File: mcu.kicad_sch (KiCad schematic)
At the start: 33 parts, among them J301 CONN_MCU_SERIAL, J302 CONN_EXT, SW301 SW_RST, SW302 SW_BOOT0, U301 STM32F765IITx, Y301 25MHz

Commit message: Fully update PCB and schematic after BOM consolidation
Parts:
- C301, C302, C303, C304, C305, C306, C307, C308, C309, C310, C311, C312, C313, C314, C315, C316: Part (none) -> 603-CC603ZRY5V7BB104
- C317, C318: Part (none) -> 187-CL10A225KQ8NNNC
- C319, C320: Part (none) -> 187-CL10C120JB81PNC
- R301, R302, R303: Part (none) -> 791-RMC1/16-1002FTP
- R304: Part (none) -> 791-RMC1/16-221JTP
- R305, R306, R307: Part (none) -> 652-CR0603-J/-000ELF
- SW301, SW302: Part (none) -> 113-DTSMW-69N-V-T/R
- Y301: Part (none) -> 815-ABM3B-25-B2
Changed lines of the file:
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@@
+      (effects (font (size 1.27 1.27)) hide)
+    )
+    (property "Part" "791-RMC1/16-221JTP" (id 4) (at 125.73 166.37 0)
       (effects (font (size 1.27 1.27)) hide)
     )
@@
     )
     (property "Datasheet" "~" (id 3) (at 203.835 160.02 0)
+      (effects (font (size 1.27 1.27)) hide)
+    )
+    (property "Part" "652-CR0603-J/-000ELF" (id 4) (at 203.835 160.02 0)
       (effects (font (size 1.27 1.27)) hide)
     )
@@
       (effects (font (size 1.27 1.27)) hide)
     )
+    (property "Part" "791-RMC1/16-1002FTP" (id 4) (at 39.37 134.62 0)
+      (effects (font (size 1.27 1.27)) hide)
+    )
     (pin "1")
     (pin "2")
@@
       (effects (font (size 1.27 1.27)) hide)
     )
+    (property "Part" "791-RMC1/16-1002FTP" (id 4) (at 39.37 144.78 0)
+      (effects (font (size 1.27 1.27)) hide)
+    )
     (pin "1")
     (pin "2")
@@
       (effects (font (size 1.27 1.27)) hide)
     )
+    (property "Part" "603-CC603ZRY5V7BB104" (id 4) (at 34.29 93.98 0)
+      (effects (font (size 1.27 1.27)) hide)
+    )
     (pin "1")
     (pin "2")
@@
       (effects (font (size 1.27 1.27)) hide)
     )
+    (property "Part" "791-RMC1/16-1002FTP" (id 4) (at 39.37 139.7 0)
+      (effects (font (size 1.27 1.27)) hide)
+    )
     (pin "1")
     (pin "2")
@@
     )
     (property "Datasheet" "~" (id 3) (at 29.21 109.22 0)
+      (effects (font (size 1.27 1.27)) hide)
+    )
+    (property "Part" "603-CC603ZRY5V7BB104" (id 4) (at 29.21 109.22 0)
       (effects (font (size 1.27 1.27)) hide)
     )
@@
       (effects (font (size 1.27 1.27)) hide)
     )
+    (property "Part" "603-CC603ZRY5V7BB104" (id 4) (at 29.21 68.58 0)
+      (effects (font (size 1.27 1.27)) hide)
+    )
     (pin "1")
     (pin "2")
@@
     )
     (property "Datasheet" "~" (id 3) (at 115.57 182.88 0)
+      (effects (font (size 1.27 1.27)) hide)
+    )
+    (property "Part" "187-CL10C120JB81PNC" (id 4) (at 115.57 182.88 0)
       (effects (font (size 1.27 1.27)) hide)
     )
@@
     )
     (property "Datasheet" "~" (id 3) (at 57.15 157.48 0)
+      (effects (font (size 1.27 1.27)) hide)
+    )
+    (property "Part" "113-DTSMW-69N-V-T/R" (id 4) (at 62.23 157.48 0)
       (effects (font (size 1.27 1.27)) hide)
     )
@@
       (effects (font (size 1.27 1.27)) hide)
     )
+    (property "Part" "603-CC603ZRY5V7BB104" (id 4) (at 29.21 58.42 0)
+      (effects (font (size 1.27 1.27)) hide)
+    )
     (pin "1")
     (pin "2")
@@
       (effects (font (size 1.27 1.27)) hide)
     )
+    (property "Part" "603-CC603ZRY5V7BB104" (id 4) (at 34.29 104.14 0)
+      (effects (font (size 1.27 1.27)) hide)
+    )
     (pin "1")
     (pin "2")
@@
     )
     (property "Datasheet" "~" (id 3) (at 77.47 135.89 0)
+      (effects (font (size 1.27 1.27)) hide)
+    )
+    (property "Part" "187-CL10A225KQ8NNNC" (id 4) (at 77.47 135.89 0)
       (effects (font (size 1.27 1.27)) hide)
     )
@@
       (effects (font (size 1.27 1.27)) hide)
     )
+    (property "Part" "603-CC603ZRY5V7BB104" (id 4) (at 29.21 88.9 0)
+      (effects (font (size 1.27 1.27)) hide)
+    )
     (pin "1")
     (pin "2")
@@
       (effects (font (size 1.27 1.27)) hide)
     )
+    (property "Part" "187-CL10A225KQ8NNNC" (id 4) (at 67.31 135.89 0)
+      (effects (font (size 1.27 1.27)) hide)
+    )
     (pin "1")
     (pin "2")
@@
     )
     (property "Datasheet" "~" (id 3) (at 125.73 182.88 0)
+      (effects (font (size 1.27 1.27)) hide)
+    )
+    (property "Part" "187-CL10C120JB81PNC" (id 4) (at 125.73 182.88 0)
       (effects (font (size 1.27 1.27)) hide)
     )
@@
     )
     (property "Datasheet" "~" (id 3) (at 200.025 154.94 0)
+      (effects (font (size 1.27 1.27)) hide)
+    )
+    (property "Part" "652-CR0603-J/-000ELF" (id 4) (at 200.025 154.94 0)
       (effects (font (size 1.27 1.27)) hide)
     )
@@
       (effects (font (size 1.27 1.27)) hide)
     )
+    (property "Part" "603-CC603ZRY5V7BB104" (id 4) (at 39.37 151.13 0)
+      (effects (font (size 1.27 1.27)) hide)
+    )
     (pin "1")
     (pin "2")
@@
       (effects (font (size 1.27 1.27)) hide)
     )
+    (property "Part" "603-CC603ZRY5V7BB104" (id 4) (at 34.29 43.18 0)
+      (effects (font (size 1.27 1.27)) hide)
+    )
     (pin "1")
     (pin "2")
@@
       (effects (font (size 1.27 1.27)) hide)
     )
+    (property "Part" "603-CC603ZRY5V7BB104" (id 4) (at 34.29 114.3 0)
+      (effects (font (size 1.27 1.27)) hide)
+    )
     (pin "1")
     (pin "2")
@@
       (effects (font (size 1.27 1.27)) hide)
     )
+    (property "Part" "603-CC603ZRY5V7BB104" (id 4) (at 34.29 83.82 0)
+      (effects (font (size 1.27 1.27)) hide)
+    )
     (pin "1")
     (pin "2")
@@
     )
     (property "Datasheet" "~" (id 3) (at 29.21 99.06 0)
+      (effects (font (size 1.27 1.27)) hide)
+    )
+    (property "Part" "603-CC603ZRY5V7BB104" (id 4) (at 29.21 99.06 0)
       (effects (font (size 1.27 1.27)) hide)
     )
@@
       (effects (font (size 1.27 1.27)) hide)
     )
+    (property "Part" "603-CC603ZRY5V7BB104" (id 4) (at 34.29 53.34 0)
+      (effects (font (size 1.27 1.27)) hide)
+    )
     (pin "1")
     (pin "2")
@@
     )
     (property "Datasheet" "~" (id 3) (at 120.65 175.26 0)
+      (effects (font (size 1.27 1.27)) hide)
+    )
+    (property "Part" "815-ABM3B-25-B2" (id 4) (at 120.65 175.26 0)
       (effects (font (size 1.27 1.27)) hide)
     )
@@
       (effects (font (size 1.27 1.27)) hide)
     )
+    (property "Part" "603-CC603ZRY5V7BB104" (id 4) (at 29.21 48.26 0)
+      (effects (font (size 1.27 1.27)) hide)
+    )
     (pin "1")
     (pin "2")
@@
       (effects (font (size 1.27 1.27)) hide)
     )
+    (property "Part" "603-CC603ZRY5V7BB104" (id 4) (at 34.29 73.66 0)
+      (effects (font (size 1.27 1.27)) hide)
+    )
     (pin "1")
     (pin "2")
@@
       (effects (font (size 1.27 1.27)) hide)
     )
+    (property "Part" "603-CC603ZRY5V7BB104" (id 4) (at 29.21 78.74 0)
+      (effects (font (size 1.27 1.27)) hide)
+    )
     (pin "1")
     (pin "2")
@@
     )
     (property "Datasheet" "~" (id 3) (at 46.99 161.29 0)
+      (effects (font (size 1.27 1.27)) hide)
+    )
+    (property "Part" "113-DTSMW-69N-V-T/R" (id 4) (at 52.07 161.29 0)
       (effects (font (size 1.27 1.27)) hide)
     )
@@
       (effects (font (size 1.27 1.27)) hide)
     )
+    (property "Part" "603-CC603ZRY5V7BB104" (id 4) (at 34.29 63.5 0)
+      (effects (font (size 1.27 1.27)) hide)
+    )
     (pin "1")
     (pin "2")
@@
       (effects (font (size 1.27 1.27)) hide)
     )
+    (property "Part" "652-CR0603-J/-000ELF" (id 4) (at 203.835 149.86 0)
+      (effects (font (size 1.27 1.27)) hide)
+    )

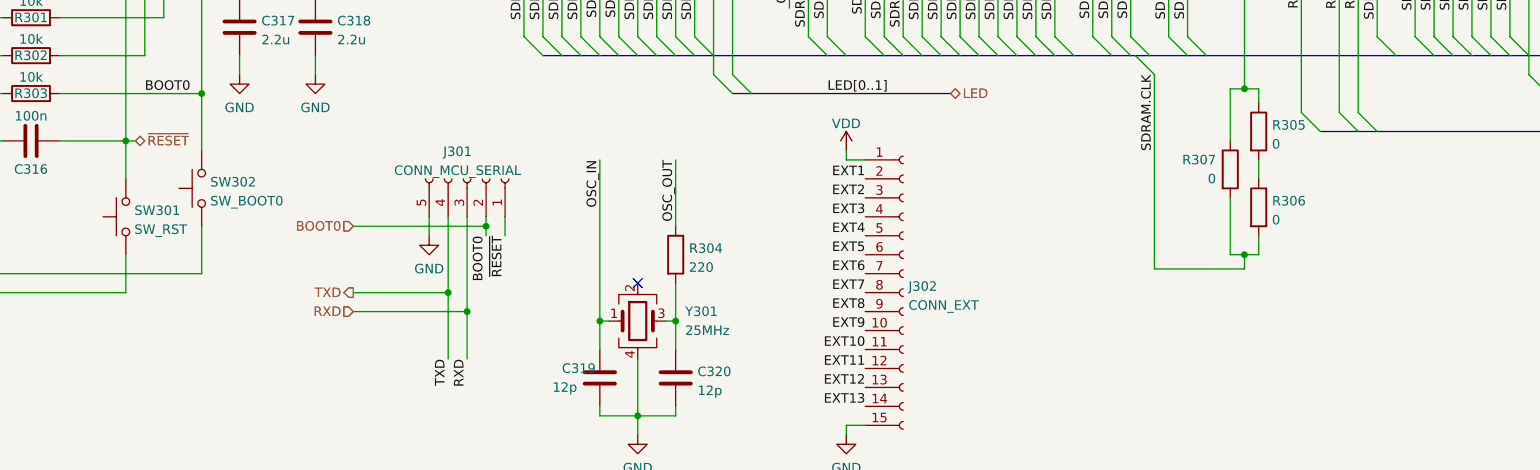
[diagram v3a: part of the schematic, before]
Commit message: Move labels on switches, jumpers and so on to a separate Label property from the Value property.
Value must be the same for components that are physically the same, otherwise it screws up the BOM. But that means we need to add each label manually.
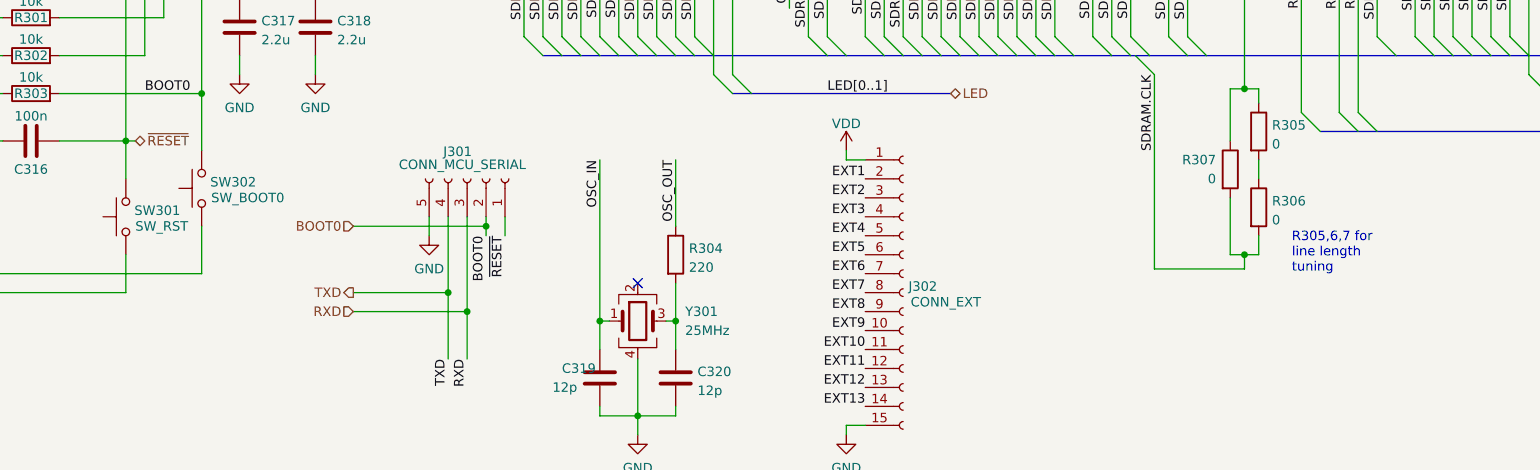
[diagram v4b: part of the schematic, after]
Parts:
- J301: value CONN_MCU_SERIAL -> PinSocket_2.54mm_1x05; Label (none) -> CONN_MCU_SERIAL
- J302: value CONN_EXT -> PinSocket_2.54mm_1x15; Label (none) -> CONN_EXT
- SW301: value SW_RST -> DTSMW69N; Label (none) -> SW_RST
- SW302: value SW_BOOT0 -> DTSMW69N; Label (none) -> SW_BOOT0
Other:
- note added: "R305,6,7 for line length tuning"
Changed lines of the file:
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@@
     (stroke (width 0) (type default) (color 0 0 0 0))
+  )
+  (text "R305,6,7 for\nline length\ntuning" (at 208.28 168.91 0)
+    (effects (font (size 1.27 1.27)) (justify left bottom))
   )
   (label "JTAG.TCK" (at 87.63 50.8 90)
@@
   )
   (symbol (lib_id "Switch:SW_Push") (at 62.23 157.48 90) (unit 1)
-    (in_bom yes) (on_board yes) (fields_autoplaced)
+    (in_bom yes) (on_board yes)
     (property "Reference" "SW302" (id 0) (at 63.373 156.6453 90)
       (effects (font (size 1.27 1.27)) (justify right))
     )
-    (property "Value" "SW_BOOT0" (id 1) (at 63.373 159.1822 90)
+    (property "Value" "DTSMW69N" (id 1) (at 63.373 159.1822 90)
+      (effects (font (size 1.27 1.27)) (justify right) hide)
+    )
+    (property "Footprint" "marco-ram-board:DTSMW69N" (id 2) (at 57.15 157.48 0)
+      (effects (font (size 1.27 1.27)) hide)
+    )
+    (property "Datasheet" "~" (id 3) (at 57.15 157.48 0)
+      (effects (font (size 1.27 1.27)) hide)
+    )
+    (property "Part" "113-DTSMW-69N-V-T/R" (id 4) (at 62.23 157.48 0)
+      (effects (font (size 1.27 1.27)) hide)
+    )
+    (property "Label" "SW_BOOT0" (id 5) (at 63.5 158.75 90)
       (effects (font (size 1.27 1.27)) (justify right))
-    )
-    (property "Footprint" "marco-ram-board:DTSMW69N" (id 2) (at 57.15 157.48 0)
-      (effects (font (size 1.27 1.27)) hide)
-    )
-    (property "Datasheet" "~" (id 3) (at 57.15 157.48 0)
-      (effects (font (size 1.27 1.27)) hide)
-    )
-    (property "Part" "113-DTSMW-69N-V-T/R" (id 4) (at 62.23 157.48 0)
-      (effects (font (size 1.27 1.27)) hide)
     )
     (pin "1")
@@
   )
   (symbol (lib_id "Connector:Conn_01x15_Female") (at 156.21 171.45 0) (unit 1)
-    (in_bom yes) (on_board yes) (fields_autoplaced)
+    (in_bom yes) (on_board yes)
     (property "Reference" "J302" (id 0) (at 156.9212 170.6153 0)
       (effects (font (size 1.27 1.27)) (justify left))
     )
-    (property "Value" "CONN_EXT" (id 1) (at 156.9212 173.1522 0)
-      (effects (font (size 1.27 1.27)) (justify left))
+    (property "Value" "PinSocket_2.54mm_1x15" (id 1) (at 156.9212 173.1522 0)
+      (effects (font (size 1.27 1.27)) (justify left) hide)
     )
     (property "Footprint" "Connector_PinSocket_2.54mm:PinSocket_1x15_P2.54mm_Vertical" (id 2) (at 156.21 171.45 0)
@@
       (effects (font (size 1.27 1.27)) hide)
     )
+    (property "Label" "CONN_EXT" (id 4) (at 161.925 172.72 0))
     (pin "1")
     (pin "10")
@@
   )
   (symbol (lib_id "Connector:Conn_01x05_Female") (at 97.79 156.21 270) (mirror x) (unit 1)
-    (in_bom yes) (on_board yes) (fields_autoplaced)
+    (in_bom yes) (on_board yes)
     (property "Reference" "J301" (id 0) (at 96.52 152.561 90))
-    (property "Value" "CONN_MCU_SERIAL" (id 1) (at 96.52 155.0979 90))
+    (property "Value" "PinSocket_2.54mm_1x05" (id 1) (at 96.52 155.0979 90)
+      (effects (font (size 1.27 1.27)) hide)
+    )
     (property "Footprint" "Connector_PinSocket_2.54mm:PinSocket_1x05_P2.54mm_Vertical" (id 2) (at 97.79 156.21 0)
       (effects (font (size 1.27 1.27)) hide)
@@
       (effects (font (size 1.27 1.27)) hide)
     )
+    (property "Label" "CONN_MCU_SERIAL" (id 4) (at 97.155 154.305 90))
     (pin "1")
     (pin "2")
@@
   )
   (symbol (lib_id "Switch:SW_Push") (at 52.07 161.29 90) (unit 1)
-    (in_bom yes) (on_board yes) (fields_autoplaced)
+    (in_bom yes) (on_board yes)
     (property "Reference" "SW301" (id 0) (at 53.213 160.4553 90)
       (effects (font (size 1.27 1.27)) (justify right))
     )
-    (property "Value" "SW_RST" (id 1) (at 53.213 162.9922 90)
+    (property "Value" "DTSMW69N" (id 1) (at 53.213 162.9922 90)
+      (effects (font (size 1.27 1.27)) (justify right) hide)
+    )
+    (property "Footprint" "marco-ram-board:DTSMW69N" (id 2) (at 46.99 161.29 0)
+      (effects (font (size 1.27 1.27)) hide)
+    )
+    (property "Datasheet" "~" (id 3) (at 46.99 161.29 0)
+      (effects (font (size 1.27 1.27)) hide)
+    )
+    (property "Part" "113-DTSMW-69N-V-T/R" (id 4) (at 52.07 161.29 0)
+      (effects (font (size 1.27 1.27)) hide)
+    )
+    (property "Label" "SW_RST" (id 5) (at 53.34 162.56 90)
       (effects (font (size 1.27 1.27)) (justify right))
     )
-    (property "Footprint" "marco-ram-board:DTSMW69N" (id 2) (at 46.99 161.29 0)
-      (effects (font (size 1.27 1.27)) hide)
-    )
-    (property "Datasheet" "~" (id 3) (at 46.99 161.29 0)
-      (effects (font (size 1.27 1.27)) hide)
-    )
-    (property "Part" "113-DTSMW-69N-V-T/R" (id 4) (at 52.07 161.29 0)
-      (effects (font (size 1.27 1.27)) hide)
-    )
-    (pin "1")
+    (pin "1")
